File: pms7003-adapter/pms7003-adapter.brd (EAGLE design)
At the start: 10.7 x 13.8 mm, 2 parts, among them J1 20021321-00010C4LF

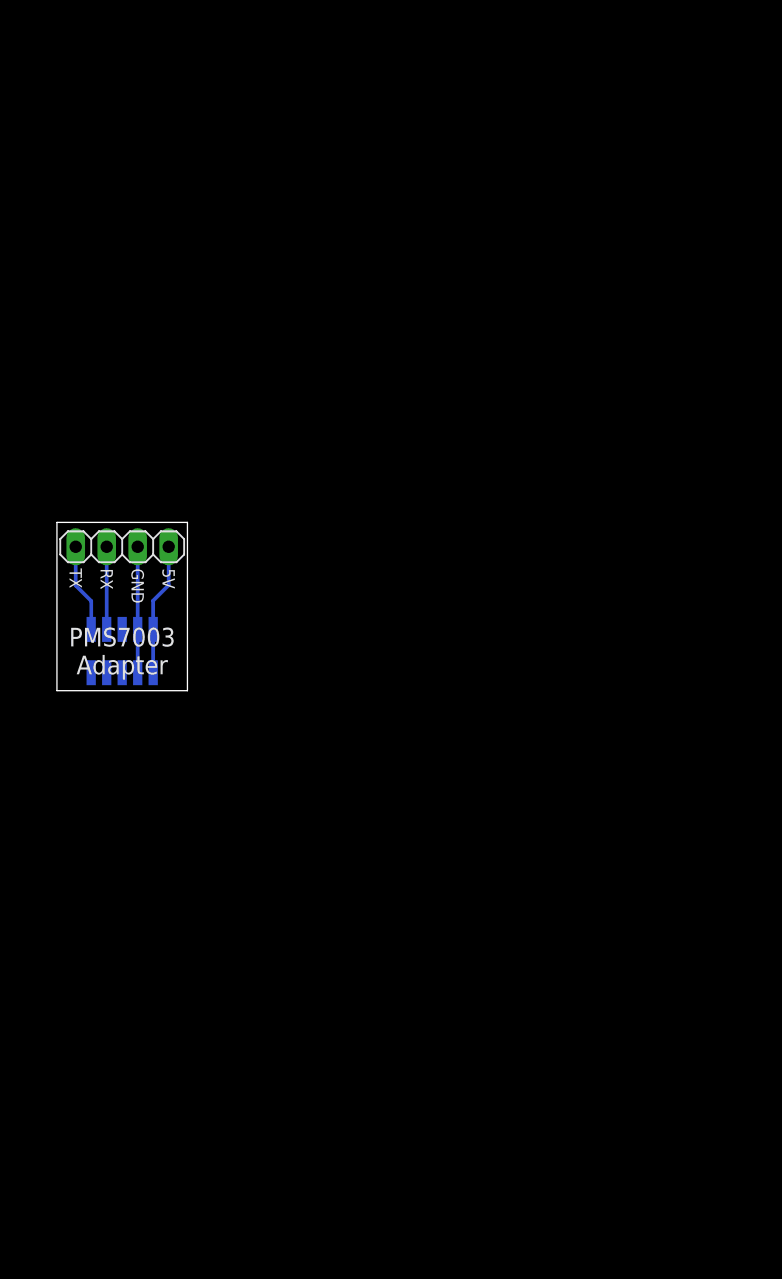
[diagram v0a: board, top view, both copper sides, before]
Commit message: Started integrating WiFi into the PMS adapter board
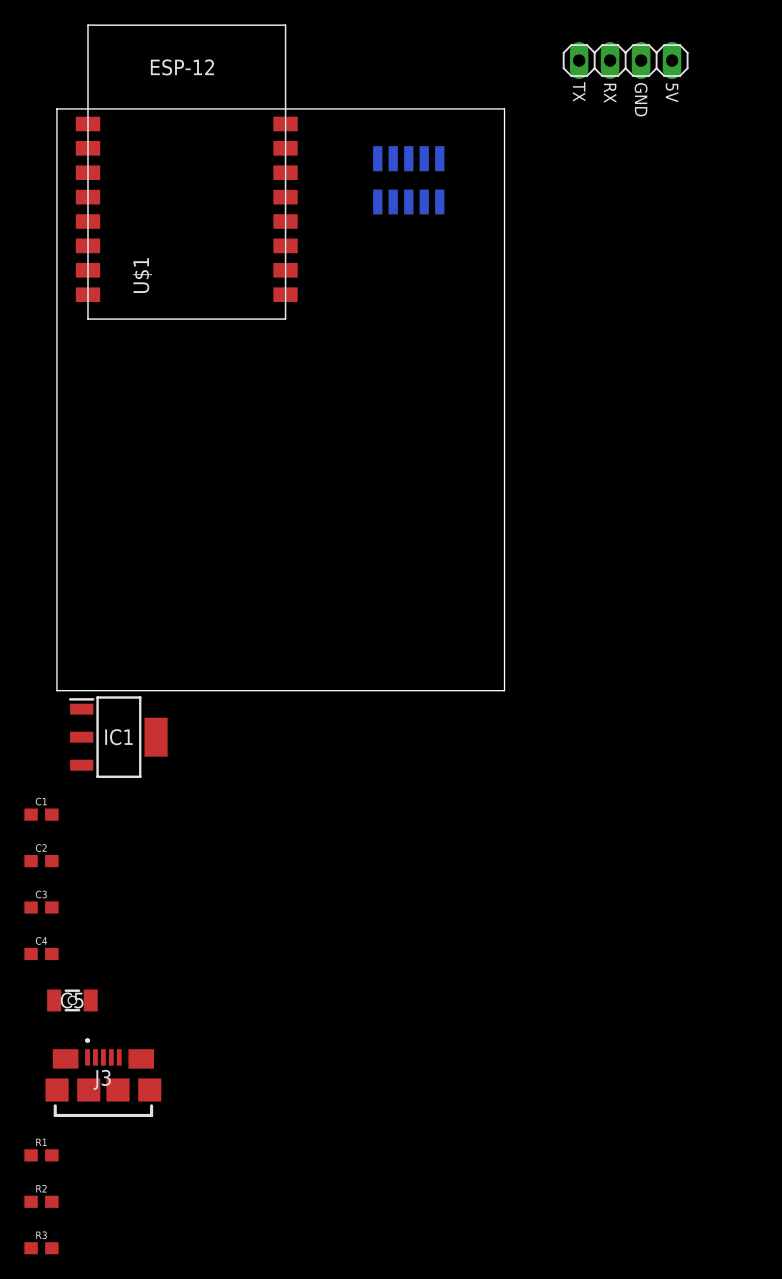
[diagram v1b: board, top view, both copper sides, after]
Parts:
- added C1, C2, C3: 4.7uF, SparkFun-Capacitors:0603
- added C4: 0.1uF, SparkFun-Capacitors:0603
- added C5: 100uF, aqm-parts:CAPC3216X180N
- added IC1: AP2114H-3.3TRG1, aqm-parts:SOT230P700X180-4N
- added J3: 10118192-0001LF, aqm-parts:101181920001LF
- added R1, R2, R3: 10k, SparkFun-Resistors:0603
- added U$1: ESP8266_ESP-12, aqm-parts:ESP8266-ESP12
- moved J2 57.4 mm to (46.6, 51.7)
- moved J1 45.2 mm to (28.9, 41.9)
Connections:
- new net 3.3V: C1.1, C3.1, C4.1, C5.1, IC1.2, IC1.4, R1.2, R2.2, R3.2, U$1.16
- new net N$1: R3.1, U$1.4
- new net N$2: R2.1, U$1.9
- new net N$3: R1.1, U$1.11
- net 5V: now also C2.1, IC1.3, J3.5
- net GND: now also C1.2, C2.2, C3.2, C4.2, C5.2, IC1.1, J3.1, U$1.1
- net RX: now also U$1.7
- net TX: now also U$1.8
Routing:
- net 5V: track 10.9 -> 0.00 mm
- net GND: track 10.3 -> 0.00 mm
- net TX: track 7.30 -> 0.00 mm
- net RX: track 6.78 -> 0.00 mm
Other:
- board size 10.7 x 13.8 mm -> 36.7 x 47.7 mm
- board text removed: "PMS7003 Adapter"

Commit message: Returned to modular design, no cables needed
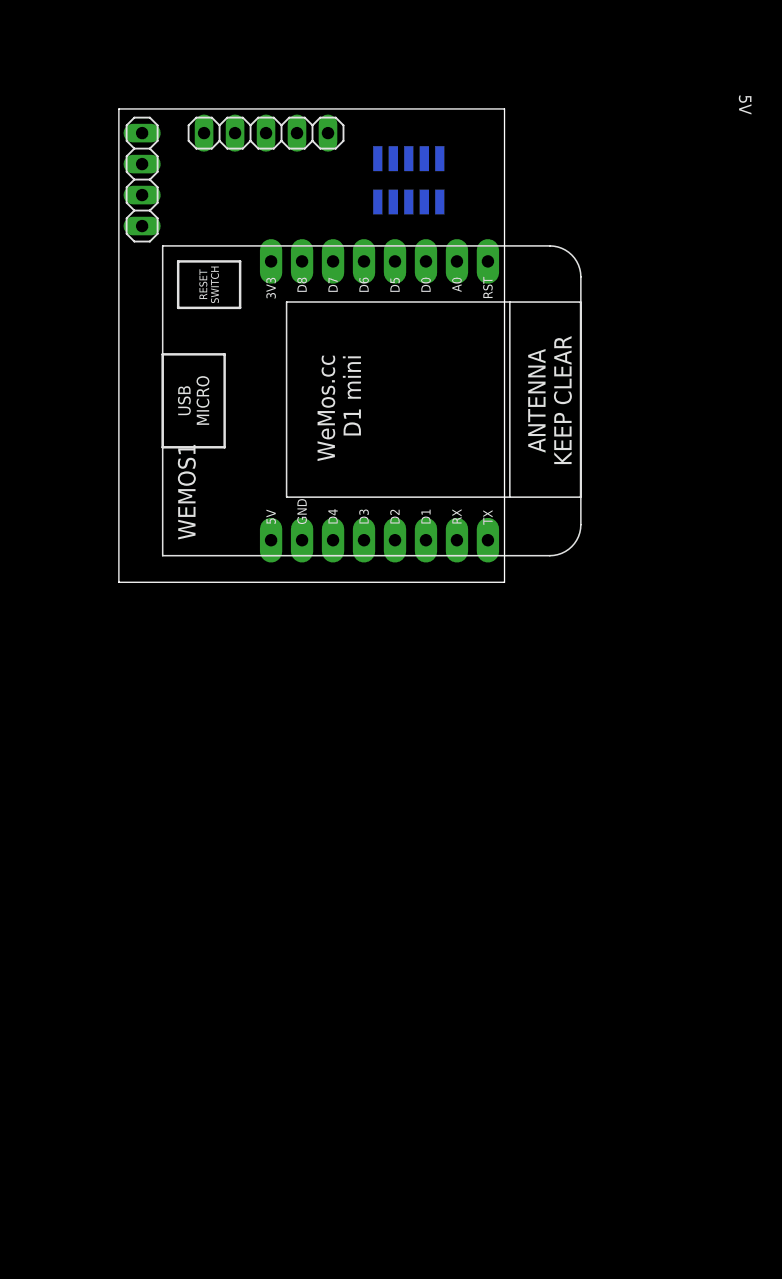
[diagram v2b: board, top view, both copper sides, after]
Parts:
- removed C1, C2, C3: 4.7uF, SparkFun-Capacitors:0603
- removed C4: 0.1uF, SparkFun-Capacitors:0603
- removed C5: 100uF, aqm-parts:CAPC3216X180N
- removed IC1: AP2114H-3.3TRG1, aqm-parts:SOT230P700X180-4N
- removed J3: 10118192-0001LF, aqm-parts:101181920001LF
- removed R1, R2, R3: 10k, SparkFun-Resistors:0603
- removed U$1: ESP8266_ESP-12, aqm-parts:ESP8266-ESP12
- added JP1: (no value), pinhead:1X05
- added WEMOS1: (no value), aqm-parts:WEMOS-D1-MINI
- moved J2 40.8 mm to (6.99, 41.9), turned to 270 degrees
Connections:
- removed net 3.3V: C1.1, C3.1, C4.1, C5.1, IC1.2, IC1.4, R1.2, R2.2, R3.2, U$1.16
- removed net N$1: R3.1, U$1.4
- removed net N$2: R2.1, U$1.9
- removed net N$3: R1.1, U$1.11
- new net SCL: J2.2, JP1.3
- new net SDA: J2.1, JP1.2
- net 5V: now also J2.4, JP1.1; no longer C2.1, IC1.3, J2.1, J3.5
- net GND: now also J2.3, JP1.5; no longer C1.2, C2.2, C3.2, C4.2, C5.2, IC1.1, J2.2, J3.1, U$1.1
- net RX: no longer J2.3, U$1.7
- net TX: no longer J2.4, U$1.8
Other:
- board size 36.7 x 47.7 mm -> 31.6 x 38.8 mm
- board text removed: "GND"
- board text removed: "RX"
- board text removed: "TX"

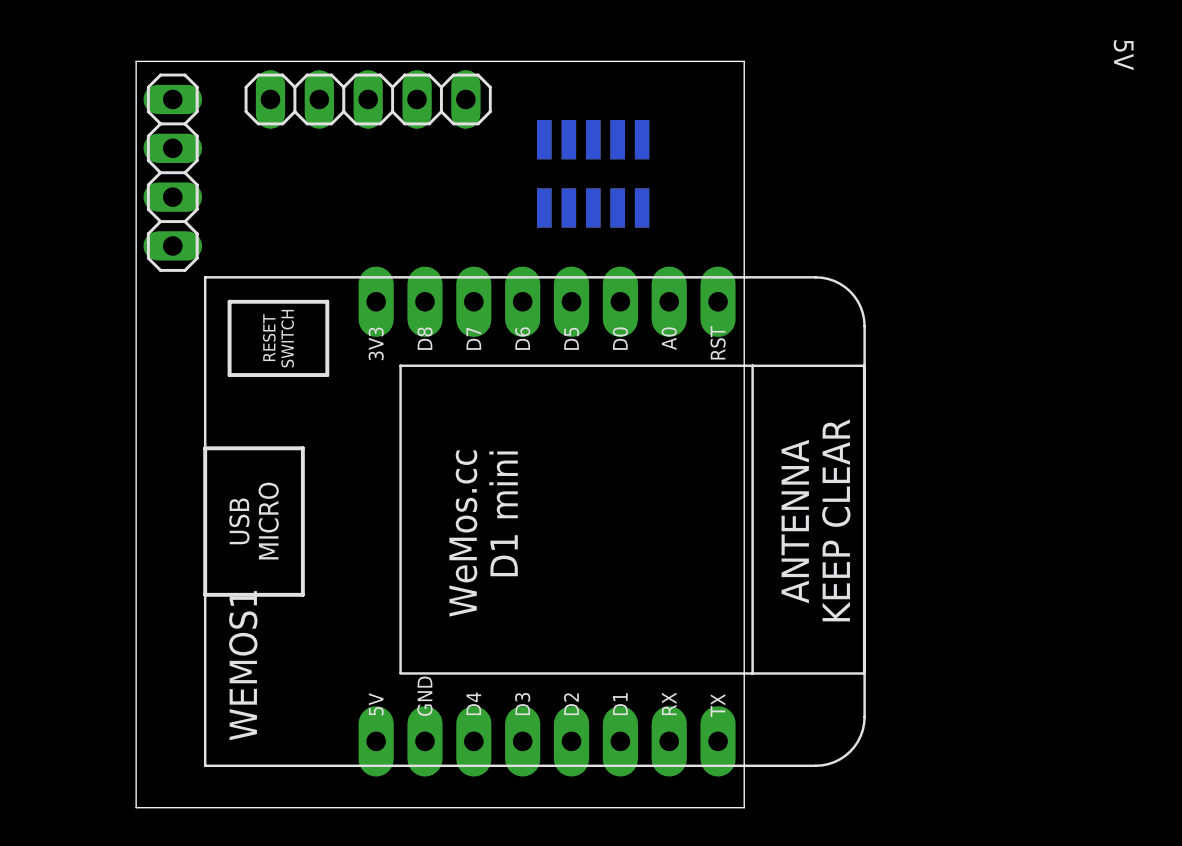
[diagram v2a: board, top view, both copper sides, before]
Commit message: Optimized design size with D1 Mini
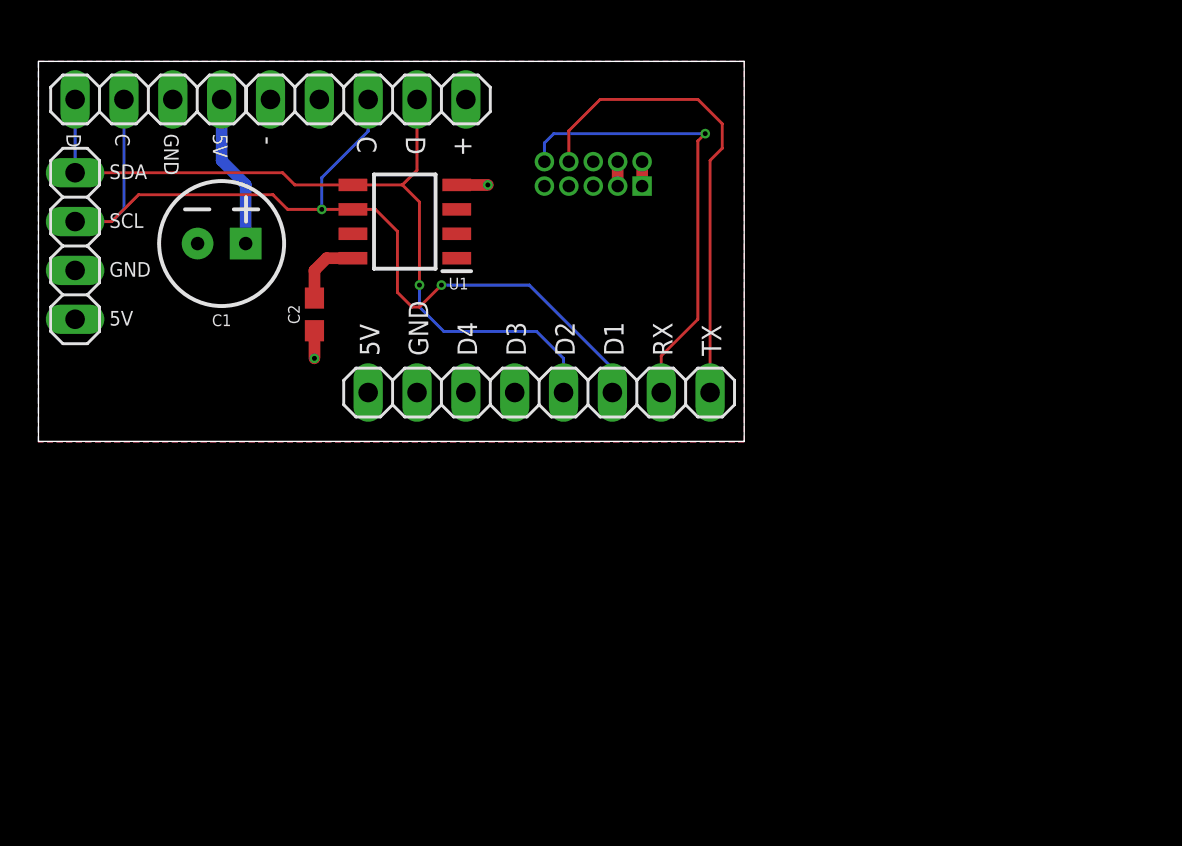
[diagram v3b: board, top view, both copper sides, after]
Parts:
- removed WEMOS1: (no value), aqm-parts:WEMOS-D1-MINI
- added C1: 100uF, SparkFun-Capacitors:CPOL-RADIAL-2.5MM-6.5MM
- added C2: 0.1uF, SparkFun-Capacitors:0603
- added J4: (no value), pinhead:1X08
- added J5: (no value), pinhead:1X04
- added U1: ATECC508A-SSHDA-T, aqm-parts:SOIC127P600X175-8N
- J1: value 20021321-00010C4LF -> LPPB052CFFN-RC; device aqm-parts:AMPHENOL_20021321-00010C4LF -> aqm-parts:SULLINS_LPPB052CFFN-RC
- moved J2 6.35 mm to (1.91, 38.1)
- turned J1 to 0 degrees
- renumbered JP1 to J3
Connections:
- removed net RX: J1.8
- removed net TX: J1.10
- new net PM_RX: J1.8, J4.1
- new net PM_TX: J1.10, J4.2
- net 5V: now also C1.1, C2.1, J4.8, J5.4, U1.8
- net GND: now also C1.2, C2.2, J4.7, J5.3, U1.4
- net SCL: now also J4.3, J5.2, U1.6
- net SDA: now also J4.4, J5.1, U1.5
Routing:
- net SCL: track 0.00 -> 51.6 mm, vias 0 -> 2
- net SDA: track 0.00 -> 42.9 mm, vias 0 -> 1
- net PM_RX: track 0.00 -> 25.0 mm
- net PM_TX: track 0.00 -> 23.9 mm, vias 0 -> 1
- net 5V: track 0.00 -> 13.0 mm
- net GND: track 0.00 -> 4.32 mm, vias 0 -> 2
- added copper zone on layer 1, net 5V
- added copper zone on layer 16, net GND
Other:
- board size 31.6 x 38.8 mm -> 36.7 x 19.8 mm
- board text added: "+"
- board text added: "-"
- board text added: "C"
- board text added: "D"
- board text added: "D1"
- board text added: "D2"
- board text added: "D3"
- board text added: "D4"
- board text added: "GND"
- board text added: "RX"
- board text added: "SCL"
- board text added: "SDA"
- board text added: "TX"
